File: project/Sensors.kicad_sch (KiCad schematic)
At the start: 19 parts, among them IC201 APDS-9306-065, IC202 BMI270, IC203 BMP581, IC204 LIS2MDLTR, IC205 BME688, Q201 DMG1013UW-7

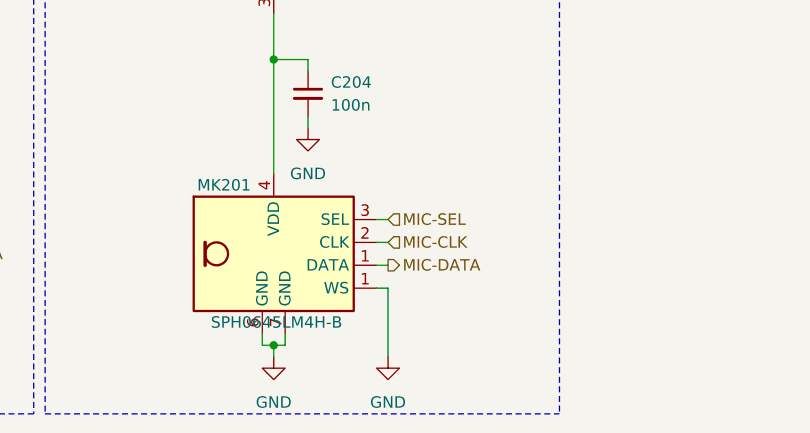
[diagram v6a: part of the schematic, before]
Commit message: - Update mic footprint
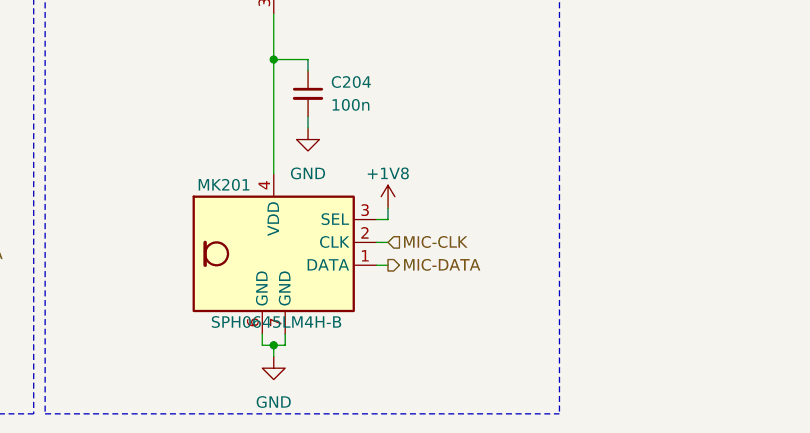
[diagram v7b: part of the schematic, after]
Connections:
- net MIC-SEL is gone; now on net +1V8: MK201.3 (SEL)
- net GND: no longer MK201.1 (WS)
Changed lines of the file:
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@@
   (no_connect (at 134.62 62.23))
   (no_connect (at 35.56 71.12))
+  (wire (pts (xy 92.71 173.99) (xy 92.71 175.26))
+    (stroke (width 0) (type default))
+  )
   (polyline (pts (xy 111.76 124.46) (xy 111.76 196.85))
     (stroke (width 0) (type dash_dot))
@@
     (stroke (width 0) (type default))
   )
-  (wire (pts (xy 92.71 182.88) (xy 92.71 190.5))
-    (stroke (width 0) (type default))
-  )
   (wire (pts (xy 238.76 22.86) (xy 238.76 24.13))
     (stroke (width 0) (type default))
@@
   )
   (wire (pts (xy 71.12 139.7) (xy 71.12 140.97))
-    (stroke (width 0) (type default))
-  )
-  (wire (pts (xy 92.71 182.88) (xy 91.44 182.88))
     (stroke (width 0) (type default))
   )
@@
     (effects (font (size 1.27 1.27)) (justify left))
   )
-  (hierarchical_label "MIC-SEL" (shape input) (at 92.71 175.26 0) (fields_autoplaced)
-    (effects (font (size 1.27 1.27)) (justify left))
-  )
   (hierarchical_label "SENSOR-SDA" (shape bidirectional) (at 33.02 63.5 180) (fields_autoplaced)
     (effects (font (size 1.27 1.27)) (justify right))
@@
         (path "/d5742f03-3b1a-42e5-a384-018bd4b919aa/82af773f-8c39-43b9-baa2-3658da6c8bb2"
           (reference "#PWR0231") (unit 1)
+        )
+      )
+    )
+  )
+  (symbol (lib_id "power:+1V8") (at 92.71 173.99 0) (unit 1)
+    (in_bom yes) (on_board yes) (dnp no) (fields_autoplaced)
+    (property "Reference" "#PWR0213" (at 92.71 177.8 0)
+      (effects (font (size 1.27 1.27)) hide)
+    )
+    (property "Value" "+1V8" (at 92.71 170.18 0)
+      (effects (font (size 1.27 1.27)))
+    )
+    (property "Footprint" "" (at 92.71 173.99 0)
+      (effects (font (size 1.27 1.27)) hide)
+    )
+    (property "Datasheet" "" (at 92.71 173.99 0)
+      (effects (font (size 1.27 1.27)) hide)
+    )
+    (pin "1")
+    (instances
+      (project "ZSWatch"
+        (path "/d5742f03-3b1a-42e5-a384-018bd4b919aa/82af773f-8c39-43b9-baa2-3658da6c8bb2"
+          (reference "#PWR0213") (unit 1)
         )
       )
@@
     )
   )
-  (symbol (lib_id "power:GND") (at 92.71 190.5 0) (unit 1)
-    (in_bom yes) (on_board yes) (dnp no)
-    (property "Reference" "#PWR0214" (at 92.71 196.85 0)
-      (effects (font (size 1.27 1.27)) hide)
-    )
-    (property "Value" "GND" (at 92.71 195.58 0)
-      (effects (font (size 1.27 1.27)))
-    )
-    (property "Footprint" "" (at 92.71 190.5 0)
-      (effects (font (size 1.27 1.27)) hide)
-    )
-    (property "Datasheet" "" (at 92.71 190.5 0)
-      (effects (font (size 1.27 1.27)) hide)
-    )
-    (pin "1")
-    (instances
-      (project "ZSWatch"
-        (path "/d5742f03-3b1a-42e5-a384-018bd4b919aa/82af773f-8c39-43b9-baa2-3658da6c8bb2"
-          (reference "#PWR0214") (unit 1)
-        )
-      )
-    )
-  )
   (symbol (lib_id "Device:C_Small") (at 44.45 36.83 0) (unit 1)
     (in_bom yes) (on_board yes) (dnp no) (fields_autoplaced)
@@
       (effects (font (size 1.27 1.27)) hide)
     )
-    (property "Datasheet" "https://www.mouser.de/datasheet/2/218/pk0641ht4h-1-rev-a-1519664.pdf" (at 80.01 179.07 0)
+    (property "Datasheet" "https://www.knowles.com/docs/default-source/default-document-library/sph0645lm4h-1-datasheet.pdf" (at 80.01 179.07 0)
       (effects (font (size 1.27 1.27)) hide)
     )
@@
     (pin "6")
     (pin "8")
-    (pin "1")
     (pin "7")
     (instances

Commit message: Some cosmetic adjustments
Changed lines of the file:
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@@
     (stroke (width 0) (type default))
   )
-  (wire (pts (xy 33.02 63.5) (xy 35.56 63.5))
+  (wire (pts (xy 34.29 63.5) (xy 35.56 63.5))
     (stroke (width 0) (type default))
   )
@@
     (stroke (width 0) (type default))
   )
-  (wire (pts (xy 34.29 181.61) (xy 36.83 181.61))
+  (wire (pts (xy 34.29 181.61) (xy 35.56 181.61))
     (stroke (width 0) (type default))
   )
@@
     (stroke (width 0) (type default))
   )
-  (wire (pts (xy 34.29 179.07) (xy 36.83 179.07))
+  (wire (pts (xy 34.29 179.07) (xy 35.56 179.07))
     (stroke (width 0) (type default))
   )
@@
     (stroke (width 0) (type default))
   )
-  (wire (pts (xy 33.02 60.96) (xy 35.56 60.96))
+  (wire (pts (xy 34.29 60.96) (xy 35.56 60.96))
     (stroke (width 0) (type default))
   )
@@
     (effects (font (size 1.27 1.27)) (justify right))
   )
-  (hierarchical_label "SENSOR-SCL" (shape input) (at 36.83 181.61 0) (fields_autoplaced)
+  (hierarchical_label "SENSOR-SCL" (shape input) (at 35.56 181.61 0) (fields_autoplaced)
     (effects (font (size 1.27 1.27)) (justify left))
   )
@@
     (effects (font (size 1.27 1.27)) (justify left))
   )
-  (hierarchical_label "SENSOR-SDA" (shape bidirectional) (at 33.02 63.5 180) (fields_autoplaced)
+  (hierarchical_label "SENSOR-SDA" (shape bidirectional) (at 34.29 63.5 180) (fields_autoplaced)
     (effects (font (size 1.27 1.27)) (justify right))
   )
@@
     (effects (font (size 1.27 1.27)) (justify left))
   )
-  (hierarchical_label "SENSOR-SCL" (shape input) (at 33.02 60.96 180) (fields_autoplaced)
-    (effects (font (size 1.27 1.27)) (justify right))
-  )
-  (hierarchical_label "SENSOR-SDA" (shape bidirectional) (at 36.83 179.07 0) (fields_autoplaced)
-    (effects (font (size 1.27 1.27)) (justify left))
-  )
+  (hierarchical_label "SENSOR-SCL" (shape input) (at 34.29 60.96 180) (fields_autoplaced)
+    (effects (font (size 1.27 1.27)) (justify right))
+  )
+  (hierarchical_label "SENSOR-SDA" (shape bidirectional) (at 35.56 179.07 0) (fields_autoplaced)
+    (effects (font (size 1.27 1.27)) (justify left))
+  )
